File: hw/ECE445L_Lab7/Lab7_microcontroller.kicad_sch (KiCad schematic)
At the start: 1 part, among them U1 EK-TM4C123GXL

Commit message: Updated hardware schematic
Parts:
- added C17, C24: 0.01uF, ECE445L:C_Axial_200mil, symbol ECE445L:C
- added C18, C21, C22, C23: 0.1uF, ECE445L:C_Axial_200mil, symbol ECE445L:C
- added C19, C27: 1uF, ECE445L:C_Axial_200mil, symbol ECE445L:C
- added C20: 2.2uF, ECE445L:CP_Radial_Tantal200mil, symbol ECE445L:C_Polarized
- added C25, C26: 10pF C0G, ECE445L:C_Axial_200mil, symbol ECE445L:C
- added J1: JTAG, ECE445L:PinHeader_1x05_P2.54mm_Vertical, symbol ECE445L:Header_5
- added R24: 1M, ECE445L:R_Axial_DIN0204_L3.6mm_D1.6mm_P7.62mm_Horizontal, symbol ECE445L:R_0.125W
- added R25: 10k, ECE445L:R_Axial_DIN0204_L3.6mm_D1.6mm_P7.62mm_Horizontal, symbol ECE445L:R_0.125W
- added SW6: Reset, Button_Switch_THT:SW_PUSH_6mm, symbol Switch:SW_Push
- added U1: TM4C123GH6PMIR, ECE445L:QFP50P1200X1200X160-64N, symbol ECE445L:TM4C123GH6PMIR
- added U11: FT2322R, symbol ECE445L:FT232RN
- added U7: ESP32-D0WD-V3, symbol ECE445L:ESP_DOIT_DEVKIT1
- added Y1: ABM3-16.000MHZ-B2-T, ECE445L:ABM3, symbol ECE445L:ABM3-16.000MHZ-B2-T
- renumbered U1 to U20
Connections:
- net +3V3: now also C17.1, C18.1, C23.1, C24.1, C27.1, R24.1, R25.1, U1.11 (VDD_1), U1.2 (VDDA), U1.26 (VDD_2), U1.37 (VBAT), U1.42 (VDD_3), U1.54 (VDD_4), U7.0 (EN), U7.29 (3V3)
- net GND: now also C17.2, C18.2, C19.2, C20.2, C21.2, C22.2, C23.2, C24.2, C25.2, C26.2, C27.2, J1.1 (A), SW6.1, U1.12 (GND_1), U1.27 (GND_2), U1.3 (GNDA), U1.34 (XOSC0), U1.35 (GNDX), U1.39 (GND_3), U1.55 (GND_4), U11.0 (GND), U7.13 (GND), U7.28 (GND)
- net PA2: now also U1.19 (PA2/SSI0C1K)
- net PA3: now also U1.20 (PA3/SSI0FSS)
- net PA4: now also U1.21 (PA4/SSI0RX)
- net PA5: now also U1.22 (PA5/SSI0TX)
- net PA6: now also U1.23 (PA6)
- net PA7: now also U1.24 (PA7)
- net PB0: now also U1.45 (PB0/USB0ID)
- net PB1: now also U1.46 (PB1/USB0VBUS)
- net PB5: now also U1.57 (PB5)
- net PB7: now also U1.4 (PB7)
- net PC4: now also U1.16 (PC4)
- net PC5: now also U1.15 (PC5)
- net PC6: now also U1.14 (PC6)
- net PC7: now also U1.13 (PC7)
- net PD2: now also U1.63 (PD2)
- net PD6: now also U1.53 (PD6)
- net PD7: now also U1.10 (PD7)
- net PE0: now also U1.9 (PE0)
- net PE1: now also U1.8 (PE1)
- net PE2: now also U1.7 (PE2)
- net PE3: now also U1.6 (PE3)
- net PE4: now also U1.59 (PE4)
- net PE5: now also U1.60 (PE5)
- net PF4: now also U1.5 (PF4)
- new net: R24.2, U1.32 (~{WAKE})
- new net ESP_IN_USB_OUT: U11.1 (RX-I), U11.2 (TX-D), U7.17 (GPIO1)
- new net ESP_OUT_USB_IN: U7.18 (GPIO3)
- new net LDO: C19.1, C20.1, C21.1, C22.1, U1.25 (VDDC_1), U1.56 (VDDC_2)
- new net OSC1: C25.1, U1.41 (OSC1), Y1.2
- new net OSC2: C26.1, U1.40 (OSC0), Y1.1
- new net PB2: U1.47 (PB2/I2C0SCL)
- new net PB3: U1.48 (PB3/I2C0SDA)
- new net PB4: U1.58 (PB4)
- new net PB6: U1.1 (PB6)
- new net PD0: U1.61 (PD0)
- new net PD1: U1.62 (PD1)
- new net PD3: U1.64 (PD3)
- new net PD4: U1.43 (PD4)
- new net PD5: U1.44 (PD5)
- new net PF0: U1.28 (PF0)
- new net PF1: U1.29 (PF1)
- new net PF2: U1.30 (PF2)
- new net PF3: U1.31 (PF3)
- new net RAUDIO_CLK: U7.12 (GPIO13), U7.8 (GPIO26)
- new net RAUDIO_FS: U7.10 (GPIO14), U7.9 (GPIO27)
- new net RAUDIO_OUT: U7.11 (GPIO12), U7.7 (GPIO25)
- new net Reset: R25.2, SW6.2, U1.38 (~{RST})
- new net TCK: J1.2 (B), U1.52 (PC0/TCK/SWCLK)
- new net TDI: J1.4 (C), U1.50 (PC2/TDI)
- new net TDO: J1.5 (C), U1.49 (PC3/TDO/SWO)
- new net TM4C_IN_ESP_OUT: U1.17 (PA0/U0RX), U7.23 (GPIO17)
- new net TM4C_OUT_ESP_IN: U1.18 (PA1/U0TX), U7.24 (GPIO16)
- new net TMS: J1.3 (C), U1.51 (PC1/TMS/SWDIO)
- no-connect marks 19 -> 22
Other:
- moved on the sheet: U20

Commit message: More Updates to hardware
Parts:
- renumbered U7 to U2, U11 to U3
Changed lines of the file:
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@@
 		(dnp no)
 		(fields_autoplaced yes)
-		(property "Reference" "U7"
+		(property "Reference" "U2"
 			(at 83.82 29.21 0)
 			(effects
@@
 			(project ""
 				(path "/69b823fd-c065-40ff-9bb9-c5835555f3eb/c4445928-c95f-4ef5-82c7-58ae1ba9c5bb"
-					(reference "U7")
+					(reference "U2")
 					(unit 1)
 				)
@@
 		(dnp no)
 		(fields_autoplaced yes)
-		(property "Reference" "U11"
-			(at 127.635 161.925 0)
+		(property "Reference" "U3"
+			(at 127.635 162.56 0)
 			(effects
 				(font
@@
 		)
 		(property "Value" "FT2322R"
-			(at 127.635 164.465 0)
+			(at 127.635 165.1 0)
 			(effects
 				(font
@@
 			(project ""
 				(path "/69b823fd-c065-40ff-9bb9-c5835555f3eb/c4445928-c95f-4ef5-82c7-58ae1ba9c5bb"
-					(reference "U11")
+					(reference "U3")
 					(unit 1)
 				)

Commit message: Lab7A Schematic and BOM - Ashton
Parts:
- renumbered C18 to C1, C26 to C10, C27 to C11, C22 to C2, C21 to C3, C23 to C4, C19 to C5, C24 to C6, C17 to C7, C20 to C8, C25 to C9, U20 to J4, R25 to R63, R24 to R64, SW6 to SW7
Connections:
- net GND: now also J4.J2_1 (GND)
- net PB2: now also J4.J2_2 (PB2)
- net PB3: now also J4.J4_3 (PB3)
- net PB4: now also J4.J1_7 (PB4)
- net PB5: now also J4.J1_2 (PB5)
- net PB6: now also J4.J2_7 (PB6)
- net PB7: now also J4.J2_6 (PB7)
- net PD0: now also J4.J3_3 (PD0)
- net PD1: now also J4.J3_4 (PD1)
- net PD2: now also J4.J3_5 (PD2)
- net PD3: now also J4.J3_6 (PD3)
- net PD6: now also J4.J4_8 (PD6)
- net PD7: now also J4.J4_9 (PD7)
- net PE3: now also J4.J3_9 (PE3)
- net PF0: now also J4.J2_4 (PF0)
- net PF1: now also J4.J3_10 (PF1)
- net PF2: now also J4.J4_1 (PF2)
- net PF3: now also J4.J4_2 (PF3)
- net RAUDIO_CLK: no longer U2.12 (GPIO13)
- net RAUDIO_FS: no longer U2.10 (GPIO14)
- net RAUDIO_OUT: no longer U2.11 (GPIO12)
- net +5V: no longer names the net of J4.J3_1 (+VBUS)
- new net LAUDIO_CLK: U2.12 (GPIO13)
- new net LAUDIO_FS: U2.10 (GPIO14)
- new net LAUDIO_OUT: U2.11 (GPIO12)
- no-connect marks 22 -> 21
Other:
- note added: "Work on pinout"
- note removed: "PB2"
- note removed: "PB3"
- note removed: "PB4"
- note removed: "PB6"
- note removed: "PD0"
- note removed: "PD1"
- note removed: "PD3"
- note removed: "PF0"
- note removed: "PF1"
- note removed: "PF2"
- note removed: "PF3"
- note removed: "~{RST}"

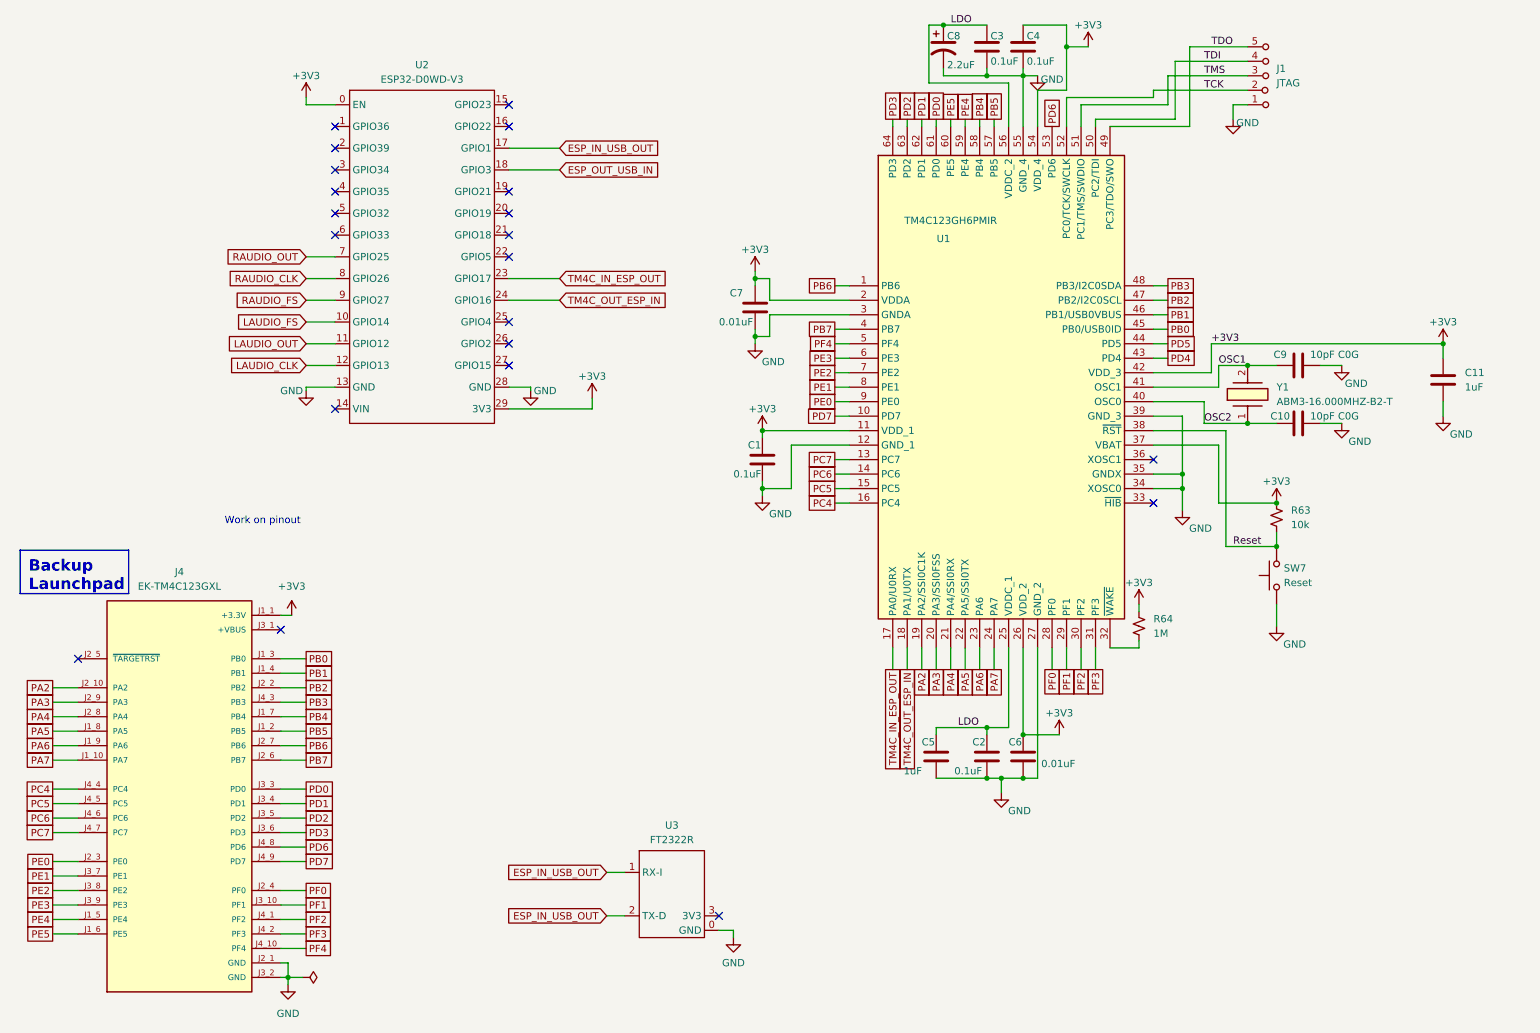
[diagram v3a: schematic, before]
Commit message: Made changers to the schematic, updated bom, and created priliminary layout for the PCB. Ready for 7B Prep!
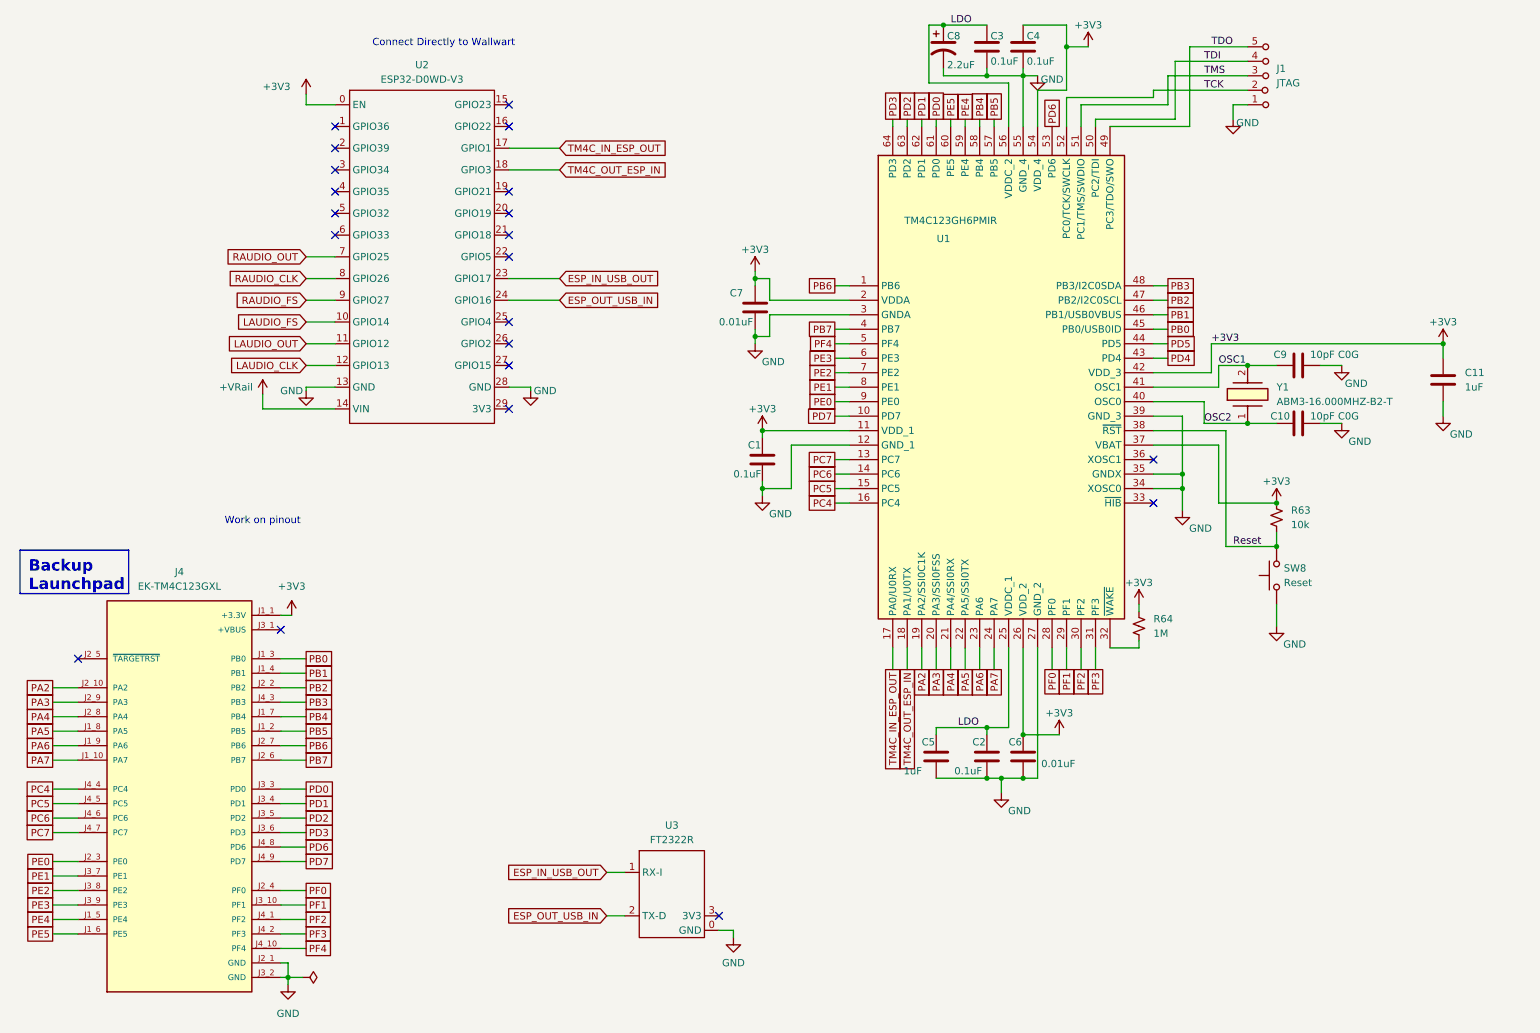
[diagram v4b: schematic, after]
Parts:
- C1, C10, C11, C2, C3, C4, C5, C6, C7, C9: footprint ECE445L:C_Axial_200mil -> Capacitor_SMD:C_0603_1608Metric
- C8: footprint ECE445L:CP_Radial_Tantal200mil -> Capacitor_SMD:C_1206_3216Metric
- R63, R64: footprint ECE445L:R_Axial_DIN0204_L3.6mm_D1.6mm_P7.62mm_Horizontal -> Resistor_SMD:R_0603_1608Metric
- U2: footprint (none) -> ECE445L:ESP32_30pin
- U3: footprint (none) -> Connector_PinHeader_1.00mm:PinHeader_1x04_P1.00mm_Vertical
- renumbered SW7 to SW8
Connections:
- net +3V3: no longer U2.29 (3V3)
- net ESP_IN_USB_OUT: now also U2.23 (GPIO17); no longer U2.17 (GPIO1), U3.2 (TX-D)
- net ESP_OUT_USB_IN: now also U2.24 (GPIO16), U3.2 (TX-D); no longer U2.18 (GPIO3)
- net TM4C_IN_ESP_OUT: now also U2.17 (GPIO1); no longer U2.23 (GPIO17)
- net TM4C_OUT_ESP_IN: now also U2.18 (GPIO3); no longer U2.24 (GPIO16)
- net +VRail: now reaches U2.14 (VIN)
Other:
- note added: "Connect Directly to Wallwart"

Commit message: Rough draft layout - need to remove tm4c chip
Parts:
- removed R63: 10k, Resistor_SMD:R_0603_1608Metric, symbol ECE445L:R_0.125W
- removed SW8: Reset, Button_Switch_THT:SW_PUSH_6mm, symbol Switch:SW_Push
- C10: renamed from C4; footprint Capacitor_SMD:C_0603_1608Metric -> Capacitor_SMD:C_0603_1608Metric_Pad1.08x0.95mm_HandSolder
- C11: renamed from C6; footprint Capacitor_SMD:C_0603_1608Metric -> Capacitor_SMD:C_0603_1608Metric_Pad1.08x0.95mm_HandSolder
- C12: renamed from C9; footprint Capacitor_SMD:C_0603_1608Metric -> Capacitor_SMD:C_0603_1608Metric_Pad1.08x0.95mm_HandSolder
- C13: renamed from C10; footprint Capacitor_SMD:C_0603_1608Metric -> Capacitor_SMD:C_0603_1608Metric_Pad1.08x0.95mm_HandSolder
- C14: renamed from C11; footprint Capacitor_SMD:C_0603_1608Metric -> Capacitor_SMD:C_0603_1608Metric_Pad1.08x0.95mm_HandSolder
- C4: renamed from C7; footprint Capacitor_SMD:C_0603_1608Metric -> Capacitor_SMD:C_0603_1608Metric_Pad1.08x0.95mm_HandSolder
- C5: renamed from C1; footprint Capacitor_SMD:C_0603_1608Metric -> Capacitor_SMD:C_0603_1608Metric_Pad1.08x0.95mm_HandSolder
- C6: renamed from C5; footprint Capacitor_SMD:C_0603_1608Metric -> Capacitor_SMD:C_0603_1608Metric_Pad1.08x0.95mm_HandSolder
- C7: renamed from C8; footprint Capacitor_SMD:C_1206_3216Metric -> Capacitor_SMD:C_1206_3216Metric_Pad1.33x1.80mm_HandSolder
- C8: renamed from C3; footprint Capacitor_SMD:C_0603_1608Metric -> Capacitor_SMD:C_0603_1608Metric_Pad1.08x0.95mm_HandSolder
- C9: renamed from C2; footprint Capacitor_SMD:C_0603_1608Metric -> Capacitor_SMD:C_0603_1608Metric_Pad1.08x0.95mm_HandSolder
- R6: renamed from R64; footprint Resistor_SMD:R_0603_1608Metric -> Resistor_SMD:R_0603_1608Metric_Pad0.98x0.95mm_HandSolder
- renumbered J4 to J2, J1 to J3, U2 to U3, U3 to U4, U1 to U5
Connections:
- net Reset is gone; now on net +3V3: U5.38 (~{RST})
- net +3V3: now also U3.1 (EN); no longer U3.0 (EN)
- net +VRail: now also U3.15 (VIN); no longer U3.14 (VIN)
- net ESP_IN_USB_OUT: now also U3.24 (GPIO17); no longer U3.23 (GPIO17)
- net ESP_OUT_USB_IN: now also U3.25 (GPIO16); no longer U3.24 (GPIO16)
- net GND: now also U3.14 (GND), U3.29 (GND), U4.4 (GND); no longer U3.13 (GND), U3.28 (GND), U4.0 (GND)
- net LAUDIO_CLK: now also U3.13 (GPIO13); no longer U3.12 (GPIO13)
- net LAUDIO_FS: now also U3.11 (GPIO14); no longer U3.10 (GPIO14)
- net LAUDIO_OUT: now also U3.12 (GPIO12); no longer U3.11 (GPIO12)
- net PB0: now also U3.18 (GPIO1)
- net PB1: now also U3.19 (GPIO3)
- net RAUDIO_CLK: now also U3.9 (GPIO26); no longer U3.8 (GPIO26)
- net RAUDIO_FS: now also U3.10 (GPIO27); no longer U3.9 (GPIO27)
- net RAUDIO_OUT: now also U3.8 (GPIO25); no longer U3.7 (GPIO25)
- net TM4C_IN_ESP_OUT: no longer names the net of U3.17 (GPIO22)
- net TM4C_IN_ESP_OUT: no longer U5.17 (PA0/U0RX)
- net TM4C_OUT_ESP_IN renamed PA1
- net PA1: no longer U3.18 (GPIO3)
- new net PA0: U5.17 (PA0/U0RX)
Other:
- company: (none) -> The University of Texas at Austin
- title: (none) -> ECE 445L Lab7

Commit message: Added current consumption to schematic
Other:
- note added: "TM4C Current Consumption (+3V3) 30.0 mA FT2322R Current Consumption (+5V Laptop) 15 mA ESP32 (+VRAIL) ~100 mA"
- note added: "TM4C Current Consumption: 38.1 mA TM4C Voltage : 3V3"
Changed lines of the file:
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@@
 		(comment 1 "Drawn By Ashton Knecht - atk836")
+	)
+	(text "TM4C Current Consumption (+3V3)\n30.0 mA\n\nFT2322R Current Consumption (+5V Laptop)\n15 mA\n\nESP32 (+VRAIL)\n~100 mA"
+		(exclude_from_sim no)
+		(at 93.98 132.08 0)
+		(effects
+			(font
+				(size 1.27 1.27)
+			)
+			(justify left)
+		)
+	)
+	(text "TM4C Current Consumption: 38.1 mA\nTM4C Voltage : 3V3"
+		(exclude_from_sim no)
+		(at 238.76 119.38 0)
+		(effects
+			(font
+				(size 1.27 1.27)
+			)
+		)
 	)
 	(text "Connect Directly to Wallwart "

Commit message: Updated lab7a report
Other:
- note added: "Microcontroller Sheet Current Consumption TM4C Current Consumption (+3V3) 30.0 mA FT2322R Current Consumption (+5V Laptop) 15 mA ESP32 (+VRAIL) ~100 mA"
- note removed: "TM4C Current Consumption (+3V3) 30.0 mA FT2322R Current Consumption (+5V Laptop) 15 mA ESP32 (+VRAIL) ~100 mA"
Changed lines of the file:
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@@
 		(comment 1 "Drawn By Ashton Knecht - atk836")
 	)
-	(text "TM4C Current Consumption (+3V3)\n30.0 mA\n\nFT2322R Current Consumption (+5V Laptop)\n15 mA\n\nESP32 (+VRAIL)\n~100 mA"
+	(text "Microcontroller Sheet Current Consumption\n\nTM4C Current Consumption (+3V3)\n30.0 mA\n\nFT2322R Current Consumption (+5V Laptop)\n15 mA\n\nESP32 (+VRAIL)\n~100 mA"
 		(exclude_from_sim no)
 		(at 93.98 132.08 0)

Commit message: PCB Layout
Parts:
- removed C10, C5, C8, C9: 0.1uF, Capacitor_SMD:C_0603_1608Metric_Pad1.08x0.95mm_HandSolder, symbol ECE445L:C
- removed C11, C4: 0.01uF, Capacitor_SMD:C_0603_1608Metric_Pad1.08x0.95mm_HandSolder, symbol ECE445L:C
- removed C12, C13: 10pF C0G, Capacitor_SMD:C_0603_1608Metric_Pad1.08x0.95mm_HandSolder, symbol ECE445L:C
- removed C14, C6: 1uF, Capacitor_SMD:C_0603_1608Metric_Pad1.08x0.95mm_HandSolder, symbol ECE445L:C
- removed C7: 2.2uF, Capacitor_SMD:C_1206_3216Metric_Pad1.33x1.80mm_HandSolder, symbol ECE445L:C_Polarized
- removed J3: JTAG, ECE445L:PinHeader_1x05_P2.54mm_Vertical, symbol ECE445L:Header_5
- removed R6: 1M, Resistor_SMD:R_0603_1608Metric_Pad0.98x0.95mm_HandSolder, symbol ECE445L:R_0.125W
- removed U4: FT2322R, Connector_PinHeader_1.00mm:PinHeader_1x04_P1.00mm_Vertical, symbol ECE445L:FT232RN
- removed U5: TM4C123GH6PMIR, ECE445L:QFP50P1200X1200X160-64N, symbol ECE445L:TM4C123GH6PMIR
- removed Y1: ABM3-16.000MHZ-B2-T, ECE445L:ABM3, symbol ECE445L:ABM3-16.000MHZ-B2-T
- added R114, R115, R116: 0, Resistor_SMD:R_0603_1608Metric_Pad0.98x0.95mm_HandSolder, symbol Device:R
- added U5: FT232R, symbol ECE445L:FT232R-Breakout
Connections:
- net +3V3: now also R114.1, R115.1; no longer J2.J1_1 (+3.3V)
- net +VRail: now also R116.1
- net ESP_IN_USB_OUT: now also U5.2 (TXD)
- net ESP_OUT_USB_IN: now also U5.3 (RXD)
- net GND: now also U5.4 (GND)
- net at J2.J3_1 (+VBUS): now also R116.2
- new net: R114.2, U5.1 (3V3)
- new net: J2.J1_1 (+3.3V), R115.2
- no-connect marks 21 -> 35
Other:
- note added: "Jumper for TM4C Power"
- note removed: "TM4C Current Consumption: 38.1 mA TM4C Voltage : 3V3"
- note removed: "Work on pinout"
- moved on the sheet: J2
